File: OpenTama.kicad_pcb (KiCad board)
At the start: 2 copper layers, 45 x 58.2 mm, 65 parts, among them J1 Conn_01x09, J2 Conn_01x14, J3 Conn_01x07, J4 USB_C_Receptacle_USB2.0, J5 Conn_01x14, Q1 BSS138, Q2 BSS138, Q3 BSS84, SW1 LEFT, SW2 MIDDLE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

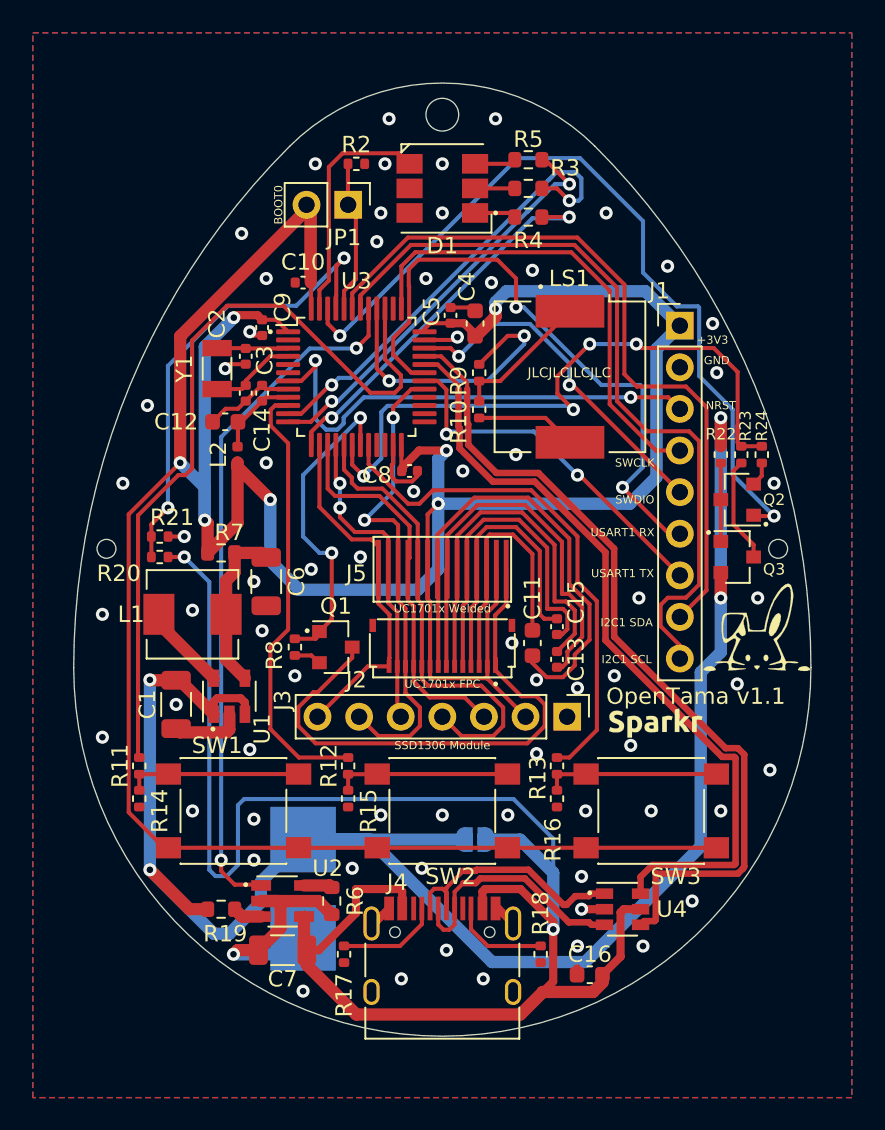
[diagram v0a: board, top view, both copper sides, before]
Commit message: Upgrade project to KiCad 7
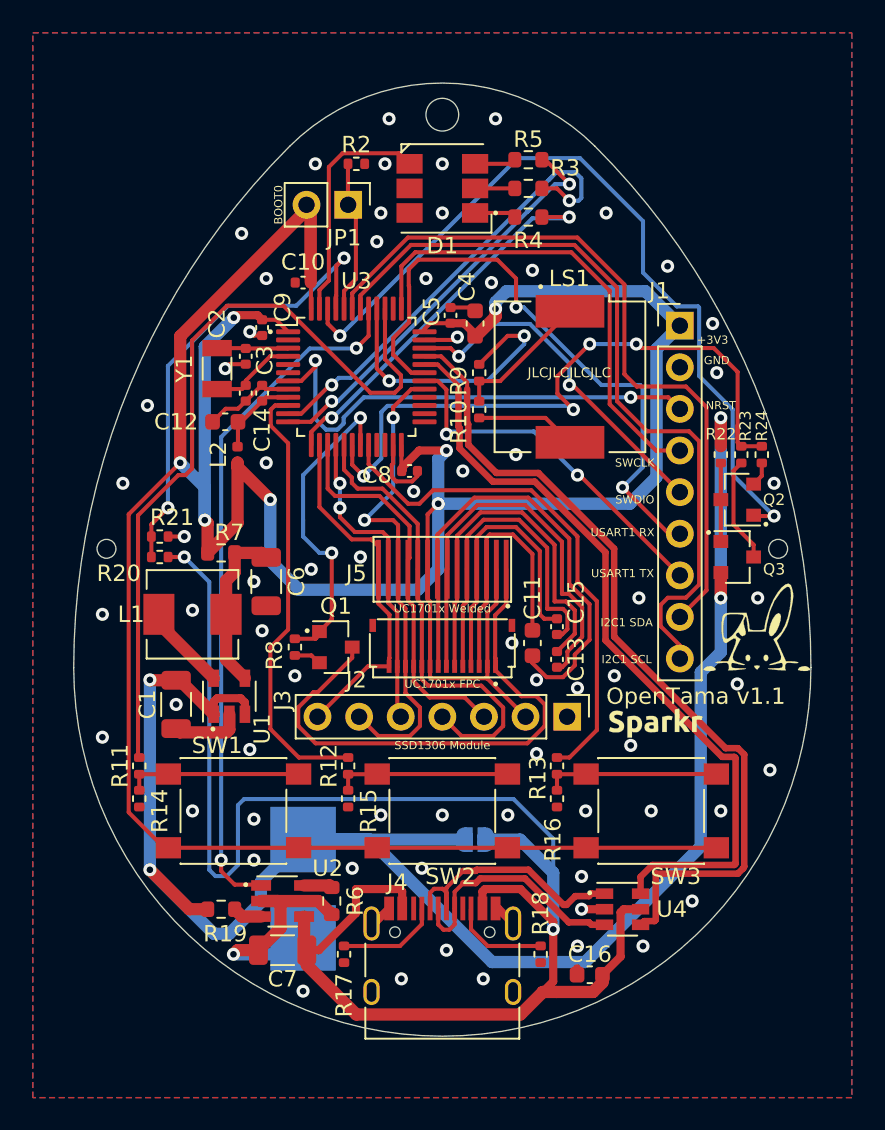
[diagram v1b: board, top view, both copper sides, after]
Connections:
- net +3V3 renamed +3.3V
- J4 pad A8: Net-(J4-PadA8) -> unconnected-(J4-SBU1-PadA8)
- J4 pad B8: Net-(J4-PadB8) -> unconnected-(J4-SBU2-PadB8)
- U3 pad 2: Net-(U3-Pad2) -> unconnected-(U3-PC13-Pad2)
- U3 pad 21: Net-(U3-Pad21) -> unconnected-(U3-PB10-Pad21)
- U3 pad 22: Net-(U3-Pad22) -> unconnected-(U3-PB11-Pad22)
- U3 pad 25: Net-(U3-Pad25) -> unconnected-(U3-PB12-Pad25)
- U3 pad 26: Net-(U3-Pad26) -> unconnected-(U3-PB13-Pad26)
- U3 pad 27: Net-(U3-Pad27) -> unconnected-(U3-PB14-Pad27)
- U3 pad 28: Net-(U3-Pad28) -> unconnected-(U3-PB15-Pad28)
- U3 pad 38: Net-(U3-Pad38) -> unconnected-(U3-PA15-Pad38)
- U3 pad 5: Net-(U3-Pad5) -> unconnected-(U3-PH0-Pad5)
- U3 pad 6: Net-(U3-Pad6) -> unconnected-(U3-PH1-Pad6)
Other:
- net class Default removed
- net class USB removed
